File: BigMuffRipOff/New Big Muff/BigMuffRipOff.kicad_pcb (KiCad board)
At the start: 4 copper layers, 59.3 x 32 mm, 70 parts, among them J1 Conn_02x08_Odd_Even, Q1 BC549, Q2 BC549, Q3 BC549, Q4 BC549, U1 TPL0501-100DCNR, U10 LM2940IMP-9.0/NOPB, U2 TPL0501-100DCNR, U3 TPL0501-100DCNR, U4 TL071HIDBVR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

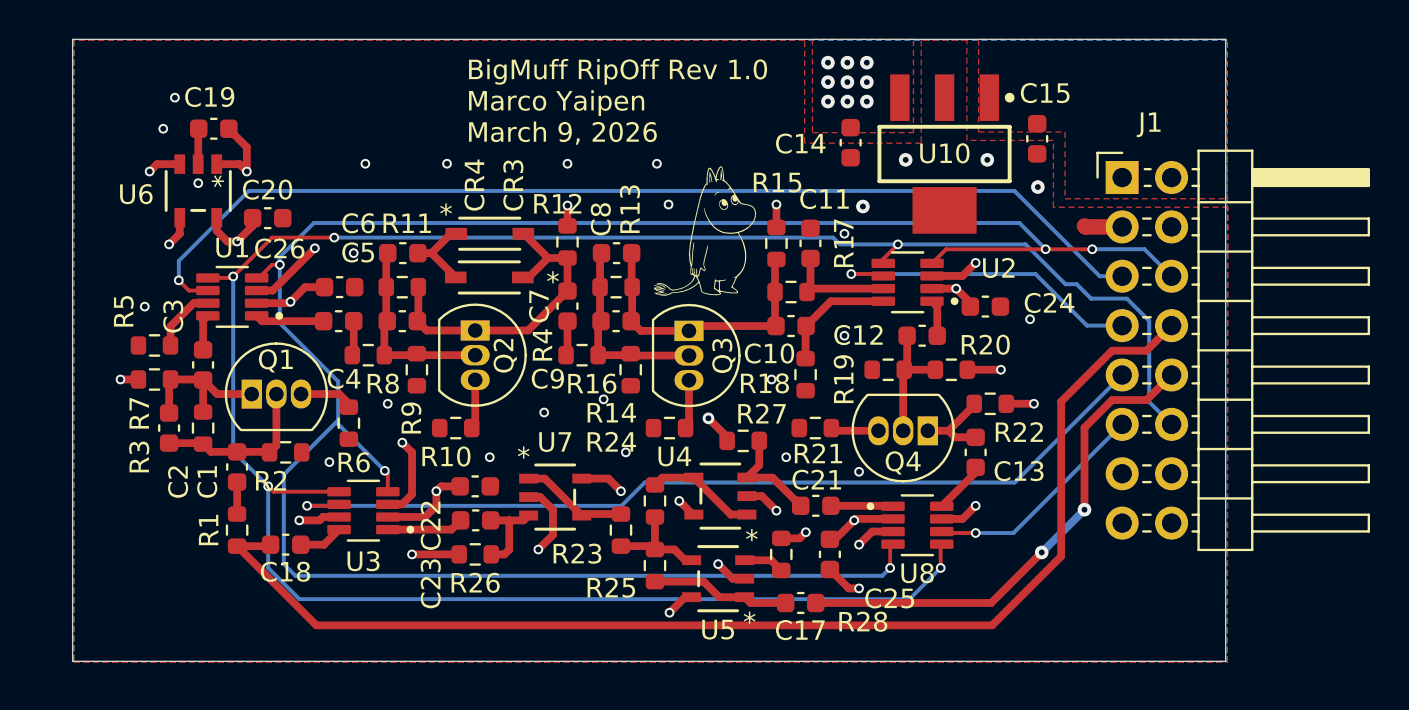
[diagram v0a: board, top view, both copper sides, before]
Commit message: connector for big muff updated
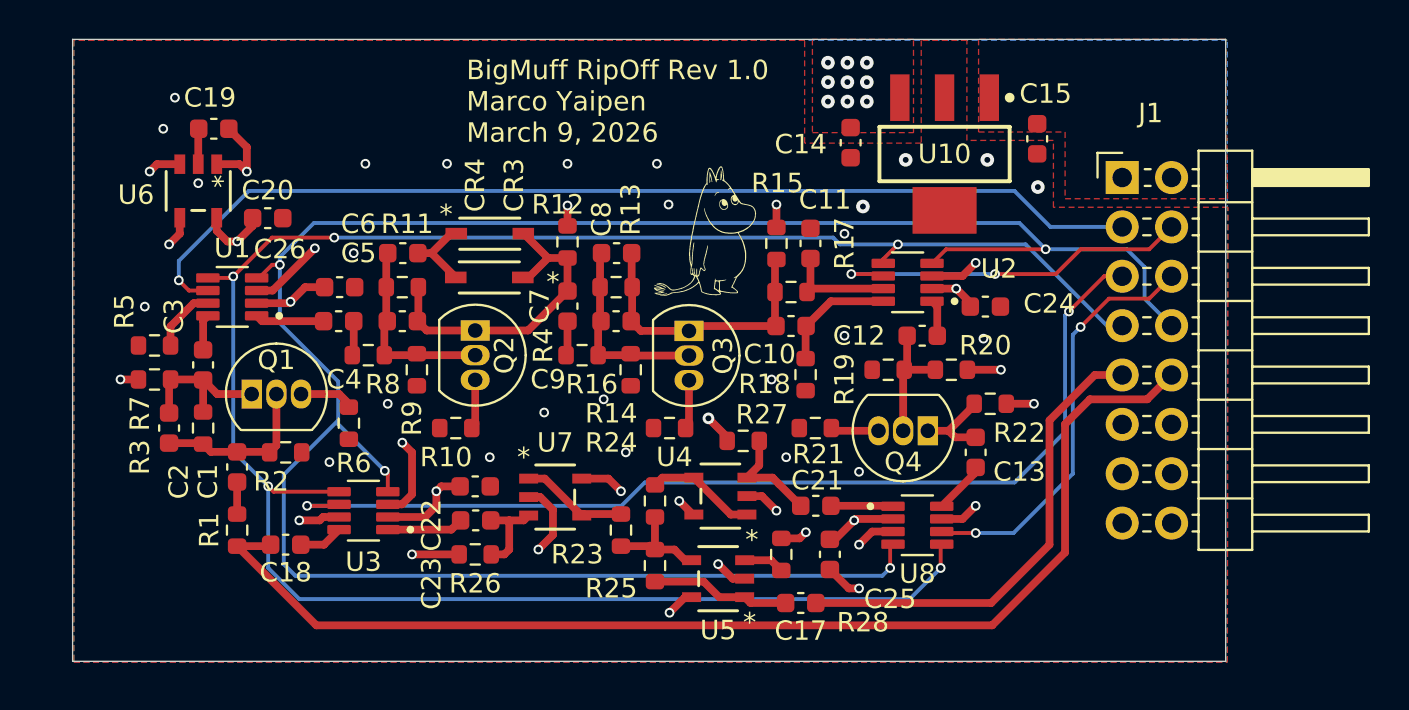
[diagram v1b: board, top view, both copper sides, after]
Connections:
- J1 pad 10: /GUITAR_OUT -> /GUITAR_IN
- J1 pad 11: /CS0 -> GND
- J1 pad 12: /MOSI -> GND
- J1 pad 3: GND -> /CS2
- J1 pad 4: GND -> /CS1
- J1 pad 5: /CS2 -> /CS3
- J1 pad 6: /SPI_CLK -> /CS0
- J1 pad 7: /CS1 -> /MOSI
- J1 pad 8: /GUITAR_IN -> /SPI_CLK
- J1 pad 9: /CS3 -> /GUITAR_OUT
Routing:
- net /CS0: track 11.6 -> 21.5 mm, vias 1 -> 2
- net /MOSI: track 114.8 -> 107.7 mm
- net /CS3: track 46.4 -> 52.0 mm, vias 1 -> 2
- net /CS1: track 16.7 -> 19.2 mm, vias 1 -> 2
- net /SPI_CLK: track 111.2 -> 113.2 mm, vias 5 -> 4
- net GND: track 30.0 -> 28.0 mm
- net /GUITAR_IN: track 62.6 -> 60.7 mm
- net /GUITAR_OUT: track 25.6 -> 24.4 mm, vias 2 -> 0
- net /CS2: track 54.6 -> 53.5 mm

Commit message: big muff connector fixed i think?
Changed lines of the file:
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@@
 	(via
 		(at 135.2 95.75)
-		(size 0.5)
+		(size 0.6)
 		(drill 0.3)
 		(layers "F.Cu" "B.Cu")
@@
 	(via
 		(at 152 92.25)
-		(size 0.5)
+		(size 0.6)
 		(drill 0.3)
 		(layers "F.Cu" "B.Cu")
@@
 	(via
 		(at 128.2 75.6)
-		(size 0.5)
+		(size 0.6)
 		(drill 0.3)
 		(layers "F.Cu" "B.Cu")
@@
 	(via
 		(at 160.25 92.5)
-		(size 0.5)
+		(size 0.6)
 		(drill 0.3)
 		(layers "F.Cu" "B.Cu")
@@
 	(via
 		(at 127.25 84.75)
-		(size 0.5)
+		(size 0.6)
 		(drill 0.3)
 		(layers "F.Cu" "B.Cu")
@@
 	(via
 		(at 163.25 86.25)
-		(size 0.5)
+		(size 0.6)
 		(drill 0.3)
 		(layers "F.Cu" "B.Cu")
@@
 	(via
 		(at 145 92.5)
-		(size 0.5)
+		(size 0.6)
 		(drill 0.3)
 		(layers "F.Cu" "B.Cu")
@@
 	(via
 		(at 159.75 95.25)
-		(size 0.5)
+		(size 0.6)
 		(drill 0.3)
 		(layers "F.Cu" "B.Cu")
@@
 	(via
 		(at 138 82)
-		(size 0.5)
+		(size 0.6)
 		(drill 0.3)
 		(layers "F.Cu" "B.Cu")
@@
 	(via
 		(at 136.75 92.75)
-		(size 0.5)
+		(size 0.6)
 		(drill 0.3)
 		(layers "F.Cu" "B.Cu")
@@
 	(via
 		(at 163.25 81)
-		(size 0.5)
+		(size 0.6)
 		(drill 0.3)
 		(layers "F.Cu" "B.Cu")
@@
 	(via
 		(at 154.2 79.5)
-		(size 0.5)
+		(size 0.6)
 		(drill 0.3)
 		(layers "F.Cu" "B.Cu")
@@
 	(via
 		(at 153.6 77.4)
-		(size 0.5)
+		(size 0.6)
 		(drill 0.3)
 		(layers "F.Cu" "B.Cu")
@@
 	(via
 		(at 142.8 77.4)
-		(size 0.5)
+		(size 0.6)
 		(drill 0.3)
 		(layers "F.Cu" "B.Cu")
@@
 	(via
 		(at 170 82.5)
-		(size 0.5)
+		(size 0.6)
 		(drill 0.3)
 		(layers "F.Cu" "B.Cu")
@@
 	(via
 		(at 149 77.4)
-		(size 0.5)
+		(size 0.6)
 		(drill 0.3)
 		(layers "F.Cu" "B.Cu")
@@
 	(via
 		(at 164 99.25)
-		(size 0.5)
+		(size 0.6)
 		(drill 0.3)
 		(layers "F.Cu" "B.Cu")
@@
 	(via
 		(at 164 97)
-		(size 0.5)
+		(size 0.6)
 		(drill 0.3)
 		(layers "F.Cu" "B.Cu")
@@
 	(via
 		(at 170 95)
-		(size 0.5)
+		(size 0.6)
 		(drill 0.3)
 		(layers "F.Cu" "B.Cu")
@@
 	(via
 		(at 147.8 90.2)
-		(size 0.5)
+		(size 0.6)
 		(drill 0.3)
 		(layers "F.Cu" "B.Cu")
@@
 	(via
 		(at 130 78.4)
-		(size 0.5)
+		(size 0.6)
 		(drill 0.3)
 		(layers "F.Cu" "B.Cu")
@@
 	(via
 		(at 139.75 89.75)
-		(size 0.5)
+		(size 0.6)
 		(drill 0.3)
 		(layers "F.Cu" "B.Cu")
@@
 	(via
 		(at 140.5 91.75)
-		(size 0.5)
+		(size 0.6)
 		(drill 0.3)
 		(layers "F.Cu" "B.Cu")
@@
 	(via
 		(at 156.75 98)
-		(size 0.5)
+		(size 0.6)
 		(drill 0.3)
 		(layers "F.Cu" "B.Cu")
@@
 	(via
 		(at 136 81.75)
-		(size 0.5)
+		(size 0.6)
 		(drill 0.3)
 		(layers "F.Cu" "B.Cu")
@@
 	(via
 		(at 147.5 97.25)
-		(size 0.5)
+		(size 0.6)
 		(drill 0.3)
 		(layers "F.Cu" "B.Cu")
@@
 	(via
 		(at 170.4 86.4)
-		(size 0.5)
+		(size 0.6)
 		(drill 0.3)
 		(layers "F.Cu" "B.Cu")
@@
 	(via
 		(at 150.860363 89.520726)
-		(size 0.5)
+		(size 0.6)
 		(drill 0.3)
 		(layers "F.Cu" "B.Cu")
@@
 	(via
 		(at 164 93.25)
-		(size 0.5)
+		(size 0.6)
 		(drill 0.3)
 		(layers "F.Cu" "B.Cu")
@@
 	(via
 		(at 128.8 74)
-		(size 0.5)
+		(size 0.6)
 		(drill 0.3)
 		(layers "F.Cu" "B.Cu")
@@
 	(via
 		(at 138.6 77.4)
-		(size 0.5)
+		(size 0.6)
 		(drill 0.3)
 		(layers "F.Cu" "B.Cu")
@@
 	(via
 		(at 159.5 88.5)
-		(size 0.5)
+		(size 0.6)
 		(drill 0.3)
 		(layers "F.Cu" "B.Cu")
@@
 	(via
 		(at 127.5 77.8)
-		(size 0.5)
+		(size 0.6)
 		(drill 0.3)
 		(layers "F.Cu" "B.Cu")
@@
 	(via
 		(at 132.5 77.8)
-		(size 0.5)
+		(size 0.6)
 		(drill 0.3)
 		(layers "F.Cu" "B.Cu")
@@
 	(via
 		(at 154.25 100.5)
-		(size 0.5)
+		(size 0.6)
 		(drill 0.3)
 		(layers "F.Cu" "B.Cu")
@@
 	(via
 		(at 126 88.5)
-		(size 0.5)
+		(size 0.6)
 		(drill 0.3)
 		(layers "F.Cu" "B.Cu")
@@
 	(via
 		(at 173 89.75)
-		(size 0.5)
+		(size 0.6)
 		(drill 0.3)
 		(layers "F.Cu" "B.Cu")
@@
 	(via
 		(at 149 79.55)
-		(size 0.5)
+		(size 0.6)
 		(drill 0.3)
 		(layers "F.Cu" "B.Cu")
@@
 	(via
 		(at 154.75 94.75)
-		(size 0.5)
+		(size 0.6)
 		(drill 0.3)
 		(layers "F.Cu" "B.Cu")
@@
 	(via
 		(at 159.75 79.5)
-		(size 0.5)
+		(size 0.6)
 		(drill 0.3)
 		(layers "F.Cu" "B.Cu")
@@
 	(via
 		(at 171.3 88)
-		(size 0.5)
+		(size 0.6)
 		(drill 0.3)
 		(layers "F.Cu" "B.Cu")
@@
 	(via
 		(at 151.75 94.25)
-		(size 0.5)
+		(size 0.6)
 		(drill 0.3)
 		(layers "F.Cu" "B.Cu")
@@
 	(via
 		(at 129 83.4)
-		(size 0.5)
+		(size 0.6)
 		(drill 0.3)
 		(layers "F.Cu" "B.Cu")
@@
 	(via
 		(at 135.6 95)
-		(size 0.5)
+		(size 0.6)
 		(drill 0.3)
 		(layers "F.Cu" "B.Cu")
@@
 	(via
 		(at 174.8 85)
-		(size 0.5)
+		(size 0.6)
 		(drill 0.3)
 		(layers "F.Cu" "B.Cu")
@@
 	(via
 		(at 131.8 83.2)
-		(size 0.5)
+		(size 0.6)
 		(drill 0.3)
 		(layers "F.Cu" "B.Cu")
@@
 	(via
 		(at 133.6 94)
-		(size 0.5)
+		(size 0.6)
 		(drill 0.3)
 		(layers "F.Cu" "B.Cu")
@@
 	(via
 		(at 166 81.551)
-		(size 0.5)
+		(size 0.6)
 		(drill 0.3)
 		(layers "F.Cu" "B.Cu")
@@
 	(via
 		(at 168.2 98.2)
-		(size 0.5)
+		(size 0.6)
 		(drill 0.3)
 		(layers "F.Cu" "B.Cu")
@@
 	(via
 		(at 137 81.2)
-		(size 0.5)
+		(size 0.6)
 		(drill 0.3)
 		(layers "F.Cu" "B.Cu")
@@
 	(via
 		(at 139.6 93.2)
-		(size 0.5)
+		(size 0.6)
 		(drill 0.3)
 		(layers "F.Cu" "B.Cu")
@@
 	(via
 		(at 134.2 82.6)
-		(size 0.5)
+		(size 0.6)
 		(drill 0.3)
 		(layers "F.Cu" "B.Cu")
@@
 	(via
 		(at 165.6 98.2)
-		(size 0.5)
+		(size 0.6)
 		(drill 0.3)
 		(layers "F.Cu" "B.Cu")
@@
 	(via
 		(at 173.6 81.8)
-		(size 0.5)
+		(size 0.6)
 		(drill 0.3)
 		(layers "F.Cu" "B.Cu")
@@
 	(via
 		(at 170 96.4)
-		(size 0.5)
+		(size 0.6)
 		(drill 0.3)
 		(layers "F.Cu" "B.Cu")
@@
 	(via
 		(at 175.4 85.8)
-		(size 0.5)
+		(size 0.6)
 		(drill 0.3)
 		(layers "F.Cu" "B.Cu")
@@
 	(via
 		(at 163.6 83.075)
-		(size 0.5)
+		(size 0.6)
 		(drill 0.3)
 		(layers "F.Cu" "B.Cu")
@@
 	(via
 		(at 171 83.075)
-		(size 0.5)
+		(size 0.6)
 		(drill 0.3)
 		(layers "F.Cu" "B.Cu")
@@
 	(via
 		(at 141 97.5)
-		(size 0.5)
+		(size 0.6)
 		(drill 0.3)
 		(layers "F.Cu" "B.Cu")
@@
 	(via
 		(at 132 81.4)
-		(size 0.5)
+		(size 0.6)
 		(drill 0.3)
 		(layers "F.Cu" "B.Cu")
@@
 	(via
 		(at 169 83.825)
-		(size 0.5)
+		(size 0.6)
 		(drill 0.3)
 		(layers "F.Cu" "B.Cu")
@@
 	(via
 		(at 142.25 94.25)
-		(size 0.5)
+		(size 0.6)
 		(drill 0.3)
 		(layers "F.Cu" "B.Cu")
@@
 	(via
 		(at 134.75 84.5)
-		(size 0.5)
+		(size 0.6)
 		(drill 0.3)
 		(layers "F.Cu" "B.Cu")
@@
 	(via
 		(at 163.75 95.75)
-		(size 0.5)
+		(size 0.6)
 		(drill 0.3)
 		(layers "F.Cu" "B.Cu")
@@
 	(via
 		(at 161.264827 96.358702)
-		(size 0.5)
+		(size 0.6)
 		(drill 0.3)
 		(layers "F.Cu" "B.Cu")
@@
 	(via
 		(at 128.5 81.55)
-		(size 0.5)
-		(drill 0.3)
-		(layers "F.Cu" "B.Cu")
+		(size 0.6)
+		(drill 0.3)
+		(layers "F.Cu" "B.Cu")

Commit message: added buffer to big muff
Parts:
- added C16: 22u, Capacitor_SMD:C_0603_1608Metric, F.Cu at (128.2, 95.0)
- added C27: 22u, Capacitor_SMD:C_0603_1608Metric, F.Cu at (132.2, 101.0)
- added C28: 1u, Capacitor_SMD:C_0603_1608Metric, B.Cu at (156.0, 95.8)
- added C29: 1u, Capacitor_SMD:C_0603_1608Metric, B.Cu at (150.0, 92.8)
- added C30: 1u, Capacitor_SMD:C_0603_1608Metric, B.Cu at (155.8, 101.0)
- added C31: 1u, Capacitor_SMD:C_0603_1608Metric, B.Cu at (129.0, 98.8)
- added R29: 500k, Resistor_SMD:R_0603_1608Metric, F.Cu at (125.0, 94.8)
- added U9: TL071HIDBVR, 284867-E-footprint:SOT23_DBV_5_TEX, F.Cu at (128.0, 99.0)
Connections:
- C18 pad 2: /GUITAR_IN -> Net-(C16-Pad2)
- R1 pad 1: /GUITAR_IN -> Net-(C16-Pad2)
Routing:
- net 4.5V: track 25.2 -> 39.1 mm
- net Net-(U9-IN+): track 0.00 -> 10.7 mm
- net Net-(U9-IN-): track 0.00 -> 6.57 mm
- net 9V: track 17.3 -> 23.8 mm, vias 19 -> 20
- net Net-(C16-Pad2): track 0.00 -> 5.62 mm
- net /GUITAR_IN: track 60.7 -> 56.4 mm
- net GND: vias 36 -> 40

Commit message: i fixed kyles fuckery
hes the goat tho
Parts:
- moved C31 2.43 mm to (131.4, 98.4), turned to 90 degrees
- moved C16 1.43 mm to (129.0, 93.8)
- moved C27 1.38 mm to (133.6, 101.0)
- moved U9 1.02 mm to (128.2, 98.0), turned to -90 degrees
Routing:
- net Net-(U9-IN+): track 10.7 -> 16.0 mm
- net GND: track 28.0 -> 29.7 mm, vias 40 -> 45
- net /GUITAR_IN: track 56.4 -> 55.0 mm
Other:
- board size 59.3 x 32 mm -> 60.9 x 32 mm
